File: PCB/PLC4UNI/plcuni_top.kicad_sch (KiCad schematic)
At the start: 28 parts, among them J1 Conn_02x08_Odd_Even, SW1 TS-1088-AR02016, SW2 TS-1088-AR02016, U18 ESP32-S3-WROOM-1, U19 ADS1115IDGS

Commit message: add ruteo buck-converter, inputs pnp,npn
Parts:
- renumbered C45 to C1, C46 to C2, C47 to C3, C38 to C4, D36 to D1, D37 to D2, D32 to D3, D33 to D4, D34 to D5, D35 to D6, R74 to R1, R75 to R2, R53 to R3, R78 to R4, R76 to R5, R54 to R6, R55 to R7, R77 to R8, TP4 to TP1, TP5 to TP2, TP6 to TP3, TP7 to TP4, U19 to U5, U18 to U6

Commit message: power supply and inputs routed
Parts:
- TP1, TP2, TP3, TP4: footprint TestPoint:TestPoint_Pad_D4.0mm -> TestPoint:TestPoint_THTPad_D1.5mm_Drill0.7mm
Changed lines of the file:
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@@
 			)
 		)
-		(property "Footprint" "TestPoint:TestPoint_Pad_D4.0mm"
+		(property "Footprint" "TestPoint:TestPoint_THTPad_D1.5mm_Drill0.7mm"
 			(at 96.52 27.94 0)
 			(hide yes)
@@
 			)
 		)
-		(property "Footprint" "TestPoint:TestPoint_Pad_D4.0mm"
+		(property "Footprint" "TestPoint:TestPoint_THTPad_D1.5mm_Drill0.7mm"
 			(at 109.22 27.94 0)
 			(hide yes)
@@
 			)
 		)
-		(property "Footprint" "TestPoint:TestPoint_Pad_D4.0mm"
+		(property "Footprint" "TestPoint:TestPoint_THTPad_D1.5mm_Drill0.7mm"
 			(at 66.04 27.94 0)
 			(hide yes)
@@
 			)
 		)
-		(property "Footprint" "TestPoint:TestPoint_Pad_D4.0mm"
+		(property "Footprint" "TestPoint:TestPoint_THTPad_D1.5mm_Drill0.7mm"
 			(at 80.01 27.94 0)
 			(hide yes)

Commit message: ruteo terminado
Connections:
- net I2C_SCK: now also U6.10 (GPIO17/U1TXD/ADC2_CH6); no longer U6.11 (GPIO18/U1RXD/ADC2_CH7/CLK_OUT3)
- net I2C_SDA: now also U6.11 (GPIO18/U1RXD/ADC2_CH7/CLK_OUT3); no longer U6.10 (GPIO17/U1TXD/ADC2_CH6)
- net IN_NPN1: now also U6.4 (GPIO4/TOUCH4/ADC1_CH3); no longer U6.22 (GPIO14/TOUCH14/ADC2_CH3/FSPIWP/FSPIDQS/SUBSPIWP)
- net IN_NPN2: now also U6.5 (GPIO5/TOUCH5/ADC1_CH4); no longer U6.39 (GPIO1/TOUCH1/ADC1_CH0)
- net IN_NPN3: now also U6.6 (GPIO6/TOUCH6/ADC1_CH5); no longer U6.38 (GPIO2/TOUCH2/ADC1_CH1)
- net IN_NPN4: now also U6.7 (GPIO7/TOUCH7/ADC1_CH6); no longer U6.15 (GPIO3/TOUCH3/ADC1_CH2)
- net IN_PNP1: now also U6.17 (GPIO9/TOUCH9/ADC1_CH8/FSPIHD/SUBSPIHD); no longer C2.1, D1.1 (K), SW2.2, U6.16 (GPIO46)
- net IN_PNP2: now also C2.1, D1.1 (K), SW2.2, U6.16 (GPIO46); no longer U6.24 (GPIO47/SPICLK_P/SUBSPICLK_P_DIFF)
- net OUT_NPN1: now also U6.39 (GPIO1/TOUCH1/ADC1_CH0); no longer U6.4 (GPIO4/TOUCH4/ADC1_CH3)
- net OUT_NPN2: now also U6.38 (GPIO2/TOUCH2/ADC1_CH1); no longer U6.5 (GPIO5/TOUCH5/ADC1_CH4)
- net OUT_NPN3: now also U6.15 (GPIO3/TOUCH3/ADC1_CH2); no longer U6.6 (GPIO6/TOUCH6/ADC1_CH5)
- net OUT_NPN4: now also U6.22 (GPIO14/TOUCH14/ADC2_CH3/FSPIWP/FSPIDQS/SUBSPIWP); no longer U6.7 (GPIO7/TOUCH7/ADC1_CH6)
- net RS485-TX: now also U6.24 (GPIO47/SPICLK_P/SUBSPICLK_P_DIFF); no longer U6.17 (GPIO9/TOUCH9/ADC1_CH8/FSPIHD/SUBSPIHD)
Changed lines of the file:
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@@
-		)
-	)
-	(label "IN_PNP1"
-		(at 222.25 238.76 180)
-		(effects
-			(font
-				(size 1.27 1.27)
-			)
-			(justify right)
 		)
 	)
@@
 		)
 	)
-	(label "IN_PNP1"
-		(at 123.19 104.14 0)
-		(effects
-			(font
-				(size 1.27 1.27)
-			)
-			(justify left)
-		)
-	)
 	(label "EN"
 		(at 152.4 77.47 0)
@@
 		)
 	)
-	(label "RS485-TX"
-		(at 274.32 138.43 0)
-		(effects
-			(font
-				(size 1.27 1.27)
-			)
-			(justify left)
-		)
-	)
-	(label "OUT_NPN4"
-		(at 274.32 133.35 0)
-		(effects
-			(font
-				(size 1.27 1.27)
-			)
-			(justify left)
-		)
-	)
 	(label "RESET"
 		(at 274.32 115.57 0)
@@
 		)
 	)
-	(label "I2C_SCK"
-		(at 274.32 156.21 0)
-		(effects
-			(font
-				(size 1.27 1.27)
-			)
-			(justify left)
-		)
-	)
 	(label "SPI_MISO"
 		(at 107.95 233.68 180)
@@
 		)
 	)
-	(label "I2C_SDA"
-		(at 274.32 153.67 0)
-		(effects
-			(font
-				(size 1.27 1.27)
-			)
-			(justify left)
-		)
-	)
 	(label "RESET"
 		(at 107.95 228.6 180)
@@
 		)
 	)
+	(label "I2C_SCK"
+		(at 274.32 153.67 0)
+		(effects
+			(font
+				(size 1.27 1.27)
+			)
+			(justify left)
+		)
+	)
+	(label "OUT_NPN1"
+		(at 274.32 118.11 0)
+		(effects
+			(font
+				(size 1.27 1.27)
+			)
+			(justify left)
+		)
+	)
 	(label "SPI_MISO"
 		(at 274.32 148.59 0)
@@
 	)
 	(label "IN_NPN3"
-		(at 274.32 120.65 0)
+		(at 274.32 130.81 0)
 		(effects
 			(font
@@
 		)
 	)
+	(label "I2C_SDA"
+		(at 274.32 156.21 0)
+		(effects
+			(font
+				(size 1.27 1.27)
+			)
+			(justify left)
+		)
+	)
 	(label "SD_CS"
 		(at 294.64 238.76 0)
@@
 		)
 	)
-	(label "IN_NPN1"
+	(label "OUT_NPN4"
 		(at 274.32 151.13 0)
-		(effects
-			(font
-				(size 1.27 1.27)
-			)
-			(justify left)
-		)
-	)
-	(label "IN_PNP2"
-		(at 274.32 168.91 0)
 		(effects
 			(font
@@
 		)
 	)
-	(label "OUT_NPN3"
-		(at 274.32 130.81 0)
-		(effects
-			(font
-				(size 1.27 1.27)
-			)
-			(justify left)
-		)
-	)
-	(label "OUT_NPN2"
-		(at 274.32 128.27 0)
-		(effects
-			(font
-				(size 1.27 1.27)
-			)
-			(justify left)
-		)
-	)
 	(label "USB+"
 		(at 129.54 238.76 0)
@@
 		)
 	)
+	(label "IN_NPN2"
+		(at 274.32 128.27 0)
+		(effects
+			(font
+				(size 1.27 1.27)
+			)
+			(justify left)
+		)
+	)
 	(label "I2C_SDA"
 		(at 144.78 39.37 0)
@@
 		)
 	)
-	(label "IN_NPN2"
-		(at 274.32 118.11 0)
-		(effects
-			(font
-				(size 1.27 1.27)
-			)
-			(justify left)
-		)
-	)
 	(label "I2C_SDA"
 		(at 129.54 231.14 0)
@@
 		)
 	)
-	(label "IN_PNP1"
-		(at 274.32 166.37 0)
-		(effects
-			(font
-				(size 1.27 1.27)
-			)
-			(justify left)
-		)
-	)
 	(label "USB-"
 		(at 274.32 110.49 0)
@@
 		)
 	)
+	(label "IN_PNP2"
+		(at 274.32 166.37 0)
+		(effects
+			(font
+				(size 1.27 1.27)
+			)
+			(justify left)
+		)
+	)
+	(label "IN_PNP1"
+		(at 274.32 138.43 0)
+		(effects
+			(font
+				(size 1.27 1.27)
+			)
+			(justify left)
+		)
+	)
 	(label "OUT_RLY2"
 		(at 274.32 161.29 0)
@@
 		)
 	)
+	(label "IN_NPN4"
+		(at 274.32 133.35 0)
+		(effects
+			(font
+				(size 1.27 1.27)
+			)
+			(justify left)
+		)
+	)
 	(label "LED_INFO"
 		(at 199.39 231.14 180)
@@
 		)
 	)
+	(label "IN_PNP2"
+		(at 222.25 238.76 180)
+		(effects
+			(font
+				(size 1.27 1.27)
+			)
+			(justify right)
+		)
+	)
 	(label "EM_TX"
 		(at 74.93 229.87 0)
@@
 		)
 	)
+	(label "RS485-TX"
+		(at 274.32 168.91 0)
+		(effects
+			(font
+				(size 1.27 1.27)
+			)
+			(justify left)
+		)
+	)
 	(label "OUT_NPN4"
 		(at 340.36 143.51 180)
@@
 		)
 	)
+	(label "IN_NPN1"
+		(at 274.32 125.73 0)
+		(effects
+			(font
+				(size 1.27 1.27)
+			)
+			(justify left)
+		)
+	)
 	(label "IN_PNP2"
 		(at 72.39 180.34 0)
@@
 		)
 	)
-	(label "IN_NPN4"
-		(at 274.32 123.19 0)
+	(label "IN_PNP2"
+		(at 123.19 104.14 0)
+		(effects
+			(font
+				(size 1.27 1.27)
+			)
+			(justify left)
+		)
+	)
+	(label "OUT_NPN2"
+		(at 274.32 120.65 0)
 		(effects
 			(font
@@
 		)
 	)
-	(label "OUT_NPN1"
-		(at 274.32 125.73 0)
-		(effects
-			(font
-				(size 1.27 1.27)
-			)
-			(justify left)
-		)
-	)
 	(label "SPI_MOSI"
 		(at 274.32 143.51 0)
@@
 		(effects
 			(font
+				(size 1.27 1.27)
+			)
+			(justify left)
+		)
+	)
+	(label "OUT_NPN3"
+		(at 274.32 123.19 0)
+		(effects
+			(font

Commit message: add mezzanini pcb
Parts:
- U6: footprint Espressif:ESP32-S3-WROOM-1 -> Espressif:ESP32-S3-WROOM-1U
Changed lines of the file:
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@@
 			)
 		)
-		(property "Footprint" "Espressif:ESP32-S3-WROOM-1"
+		(property "Footprint" "Espressif:ESP32-S3-WROOM-1U"
 			(at 226.06 184.15 0)
 			(hide yes)

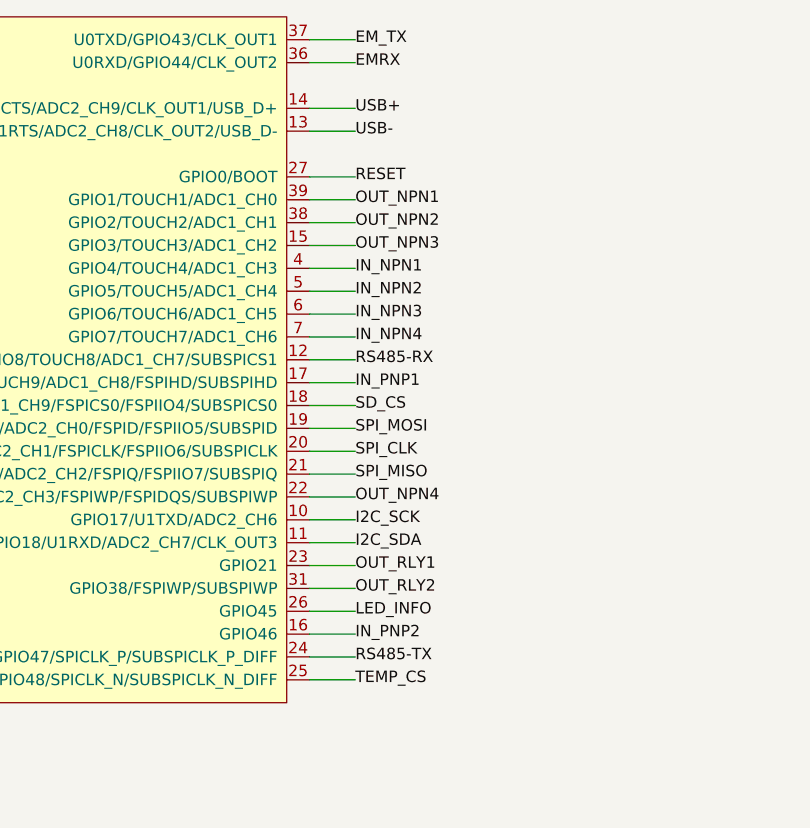
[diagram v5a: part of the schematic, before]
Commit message: re-enrrutado
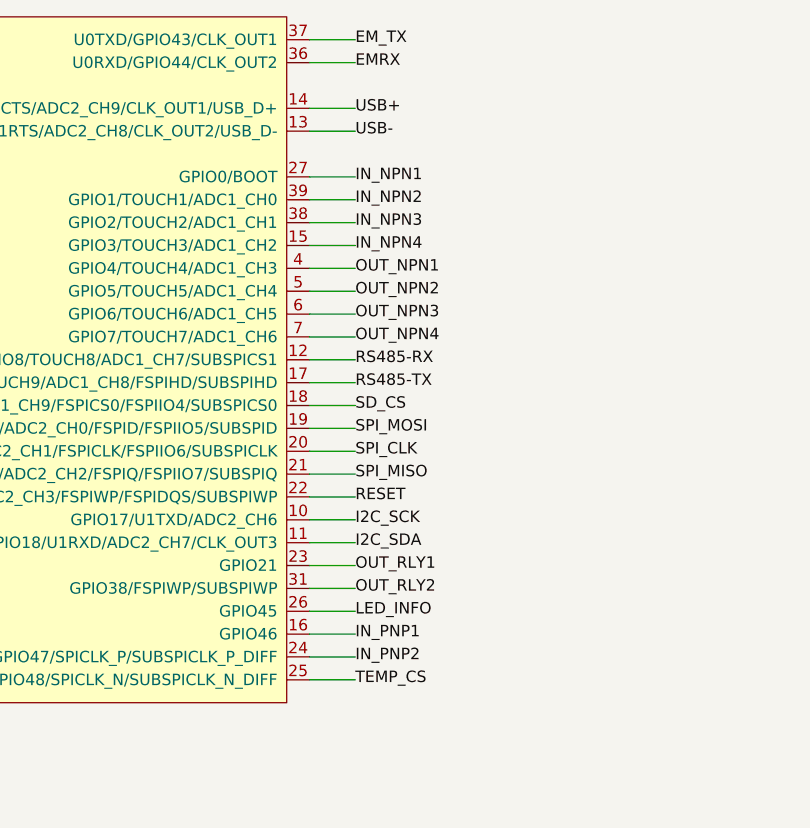
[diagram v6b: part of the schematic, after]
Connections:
- net IN_NPN1: now also U6.27 (GPIO0/BOOT); no longer U6.4 (GPIO4/TOUCH4/ADC1_CH3)
- net IN_NPN2: now also U6.39 (GPIO1/TOUCH1/ADC1_CH0); no longer U6.5 (GPIO5/TOUCH5/ADC1_CH4)
- net IN_NPN3: now also U6.38 (GPIO2/TOUCH2/ADC1_CH1); no longer U6.6 (GPIO6/TOUCH6/ADC1_CH5)
- net IN_NPN4: now also U6.15 (GPIO3/TOUCH3/ADC1_CH2); no longer U6.7 (GPIO7/TOUCH7/ADC1_CH6)
- net IN_PNP1: now also U6.16 (GPIO46); no longer U6.17 (GPIO9/TOUCH9/ADC1_CH8/FSPIHD/SUBSPIHD)
- net IN_PNP2: now also U6.24 (GPIO47/SPICLK_P/SUBSPICLK_P_DIFF); no longer U6.16 (GPIO46)
- net OUT_NPN1: now also U6.4 (GPIO4/TOUCH4/ADC1_CH3); no longer U6.39 (GPIO1/TOUCH1/ADC1_CH0)
- net OUT_NPN2: now also U6.5 (GPIO5/TOUCH5/ADC1_CH4); no longer U6.38 (GPIO2/TOUCH2/ADC1_CH1)
- net OUT_NPN3: now also U6.6 (GPIO6/TOUCH6/ADC1_CH5); no longer U6.15 (GPIO3/TOUCH3/ADC1_CH2)
- net OUT_NPN4: now also U6.7 (GPIO7/TOUCH7/ADC1_CH6); no longer U6.22 (GPIO14/TOUCH14/ADC2_CH3/FSPIWP/FSPIDQS/SUBSPIWP)
- net RESET: now also U6.22 (GPIO14/TOUCH14/ADC2_CH3/FSPIWP/FSPIDQS/SUBSPIWP); no longer U6.27 (GPIO0/BOOT)
- net RS485-TX: now also U6.17 (GPIO9/TOUCH9/ADC1_CH8/FSPIHD/SUBSPIHD); no longer U6.24 (GPIO47/SPICLK_P/SUBSPICLK_P_DIFF)
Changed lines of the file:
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@@
+		)
+	)
+	(label "IN_NPN3"
+		(at 274.32 120.65 0)
+		(effects
+			(font
+				(size 1.27 1.27)
+			)
+			(justify left)
 		)
 	)
@@
 		)
 	)
+	(label "RESET"
+		(at 274.32 151.13 0)
+		(effects
+			(font
+				(size 1.27 1.27)
+			)
+			(justify left)
+		)
+	)
+	(label "OUT_NPN1"
+		(at 274.32 125.73 0)
+		(effects
+			(font
+				(size 1.27 1.27)
+			)
+			(justify left)
+		)
+	)
 	(label "SPI_MOSI"
 		(at 288.29 238.76 180)
@@
 		)
 	)
-	(label "RESET"
-		(at 274.32 115.57 0)
+	(label "IN_NPN2"
+		(at 274.32 118.11 0)
 		(effects
 			(font
@@
 		)
 	)
+	(label "IN_PNP2"
+		(at 274.32 168.91 0)
+		(effects
+			(font
+				(size 1.27 1.27)
+			)
+			(justify left)
+		)
+	)
 	(label "RESET"
 		(at 107.95 228.6 180)
@@
 		)
 	)
-	(label "OUT_NPN1"
-		(at 274.32 118.11 0)
-		(effects
-			(font
-				(size 1.27 1.27)
-			)
-			(justify left)
-		)
-	)
 	(label "SPI_MISO"
 		(at 274.32 148.59 0)
@@
 		)
 	)
+	(label "OUT_NPN3"
+		(at 274.32 130.81 0)
+		(effects
+			(font
+				(size 1.27 1.27)
+			)
+			(justify left)
+		)
+	)
 	(label "IN_PNP1"
 		(at 72.39 166.37 0)
@@
 		)
 	)
-	(label "IN_NPN3"
-		(at 274.32 130.81 0)
-		(effects
-			(font
-				(size 1.27 1.27)
-			)
-			(justify left)
-		)
-	)
 	(label "OUT_RLY2"
 		(at 337.82 171.45 180)
@@
 		)
 	)
-	(label "OUT_NPN4"
-		(at 274.32 151.13 0)
+	(label "IN_PNP1"
+		(at 274.32 166.37 0)
 		(effects
 			(font
@@
 		)
 	)
+	(label "OUT_NPN2"
+		(at 274.32 128.27 0)
+		(effects
+			(font
+				(size 1.27 1.27)
+			)
+			(justify left)
+		)
+	)
+	(label "IN_NPN1"
+		(at 274.32 115.57 0)
+		(effects
+			(font
+				(size 1.27 1.27)
+			)
+			(justify left)
+		)
+	)
 	(label "OUT_NPN3"
 		(at 340.36 128.27 180)
@@
 		)
 	)
-	(label "IN_NPN2"
-		(at 274.32 128.27 0)
-		(effects
-			(font
-				(size 1.27 1.27)
-			)
-			(justify left)
-		)
-	)
 	(label "I2C_SDA"
 		(at 144.78 39.37 0)
@@
 		)
 	)
-	(label "IN_PNP2"
-		(at 274.32 166.37 0)
-		(effects
-			(font
-				(size 1.27 1.27)
-			)
-			(justify left)
-		)
-	)
-	(label "IN_PNP1"
-		(at 274.32 138.43 0)
-		(effects
-			(font
-				(size 1.27 1.27)
-			)
-			(justify left)
-		)
-	)
 	(label "OUT_RLY2"
 		(at 274.32 161.29 0)
@@
 		)
 	)
-	(label "IN_NPN4"
-		(at 274.32 133.35 0)
-		(effects
-			(font
-				(size 1.27 1.27)
-			)
-			(justify left)
-		)
-	)
 	(label "LED_INFO"
 		(at 199.39 231.14 180)
@@
 		)
 	)
-	(label "RS485-TX"
-		(at 274.32 168.91 0)
-		(effects
-			(font
-				(size 1.27 1.27)
-			)
-			(justify left)
-		)
-	)
 	(label "OUT_NPN4"
 		(at 340.36 143.51 180)
@@
 		)
 	)
-	(label "IN_NPN1"
-		(at 274.32 125.73 0)
-		(effects
-			(font
-				(size 1.27 1.27)
-			)
-			(justify left)
-		)
-	)
 	(label "IN_PNP2"
 		(at 72.39 180.34 0)
@@
 		)
 	)
-	(label "OUT_NPN2"
-		(at 274.32 120.65 0)
+	(label "IN_NPN4"
+		(at 274.32 123.19 0)
+		(effects
+			(font
+				(size 1.27 1.27)
+			)
+			(justify left)
+		)
+	)
+	(label "OUT_NPN4"
+		(at 274.32 133.35 0)
 		(effects
 			(font
@@
 		)
 	)
+	(label "RS485-TX"
+		(at 274.32 138.43 0)
+		(effects
+			(font
+				(size 1.27 1.27)
+			)
+			(justify left)
+		)
+	)
 	(label "SPI_CLK"
 		(at 274.32 146.05 0)
 		(effects
 			(font
-				(size 1.27 1.27)
-			)
-			(justify left)
-		)
-	)
-	(label "OUT_NPN3"
-		(at 274.32 123.19 0)
-		(effects
-			(font
